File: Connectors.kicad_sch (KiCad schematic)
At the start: 4 parts, among them J1 Conn_01x04_Pin, J2 Conn_01x04_Pin, J3 Conn_01x09_Pin, J4 Conn_02x03_Odd_Even

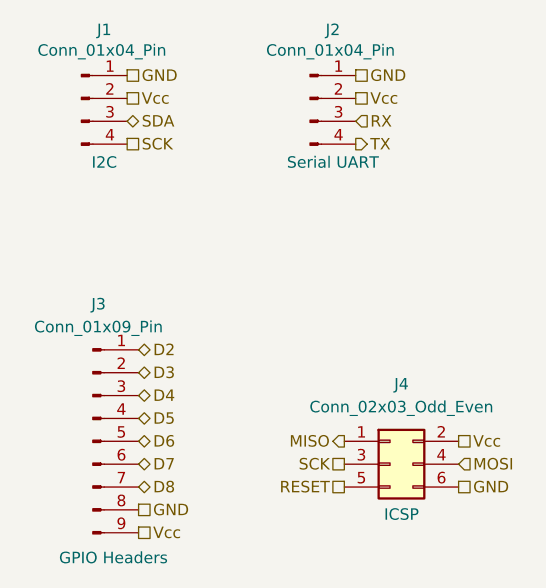
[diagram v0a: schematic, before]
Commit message: Fix Clock Bug
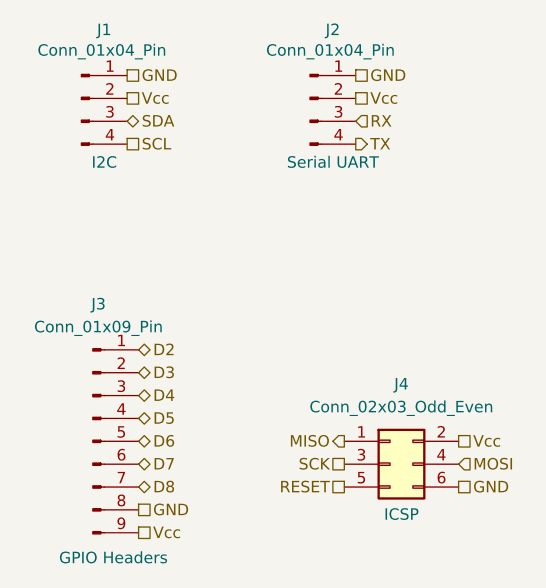
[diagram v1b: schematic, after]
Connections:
- net SCK: no longer J1.4 (Pin_4)
- new net SCL: J1.4 (Pin_4)
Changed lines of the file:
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@@
 		)
 	)
-	(hierarchical_label "SCK"
+	(hierarchical_label "SCL"
 		(shape passive)
 		(at 139.7 46.99 0)
